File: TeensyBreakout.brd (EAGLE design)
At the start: 53.3 x 68.6 mm, 74 parts, among them IC1 MCP73871

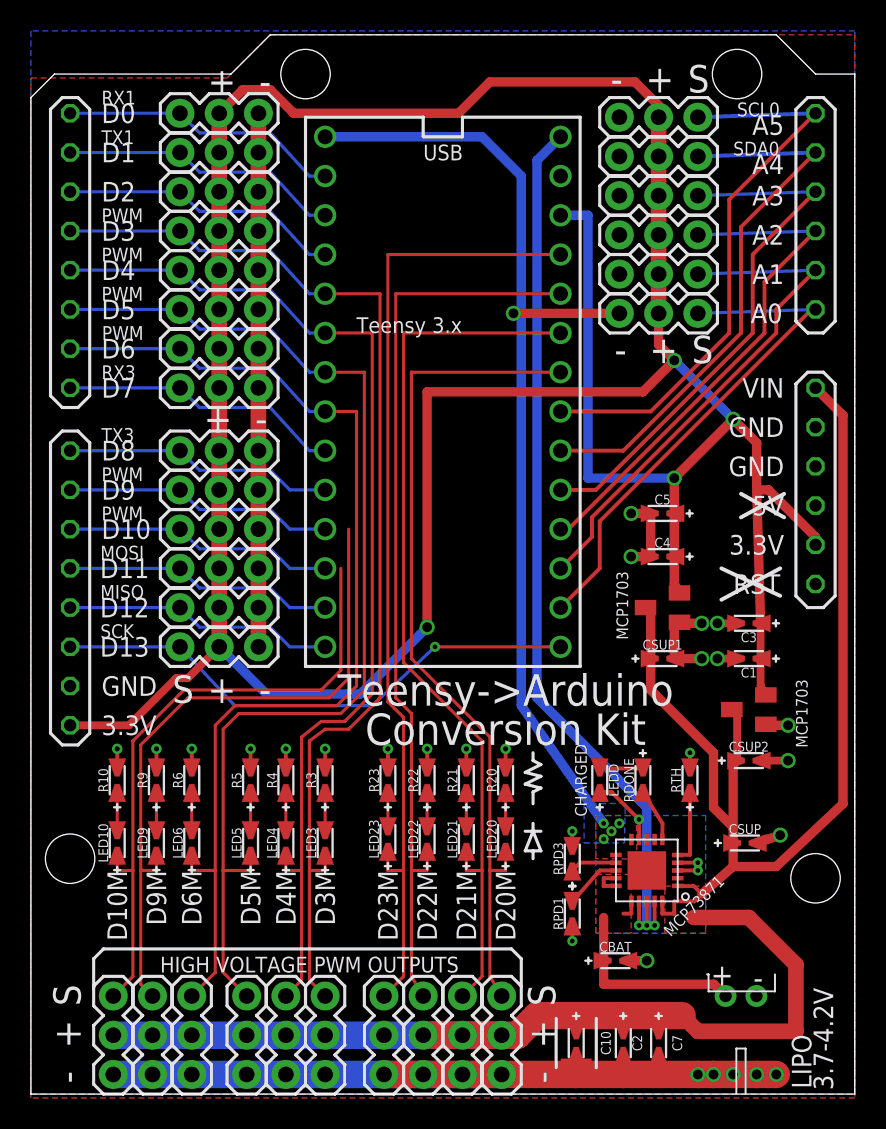
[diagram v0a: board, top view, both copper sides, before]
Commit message: Update locking headers, fix 2 missing wires
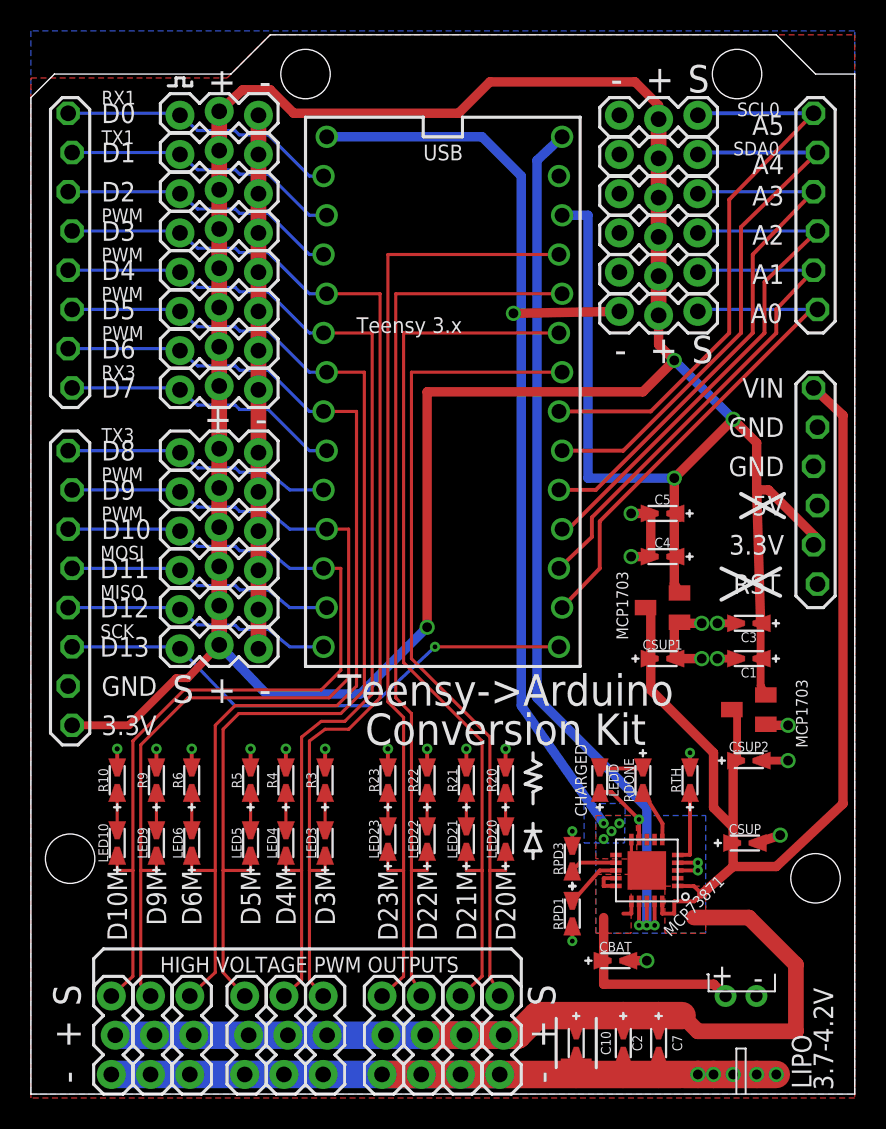
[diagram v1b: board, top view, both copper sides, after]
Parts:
- A0, A1, A2, A3, A4, A5, D0, D1, D10, D10M, D11, D12, D13, D2, D20M, D21M, D22M, D23M, D3, D3M, D4, D4M, D5, D5M, D6, D6M, D7, D8, D9, D9M: device SparkFun-Connectors:1X03 -> tekdemo:1X03_LOCK
- U$5: value TEENSY_3.1_BASIC -> TEENSY_3.1_BASICLOCK; device tekdemo:TEENSY_3.1_BASIC -> tekdemo:TEENSY_3.1_BASIC_LOCK
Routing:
- net PWM9: track 61.1 -> 62.2 mm
- net PWM10: track 58.6 -> 59.7 mm
- net GND: track 140.8 -> 141.7 mm
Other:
- board text added: "3-NOV-2015"
- board text removed: "21-OCT-2015"
